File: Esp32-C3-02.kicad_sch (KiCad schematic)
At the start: 0 parts

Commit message: Schematic update
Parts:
- added J3: GSD09002SEU, GSD09002SEU:AMPHENOL_GSD09002SEU, symbol GSD09002SEU:GSD09002SEU
- added U2: USBLC6-2SC6, Package_TO_SOT_SMD:SOT-23-6, symbol Power_Protection:USBLC6-2SC6
- added U3: ESP32-C3-WROOM-02, RF_Module:ESP32-C3-WROOM-02, symbol RF_Module:ESP32-C3-WROOM-02
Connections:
- new net: U3.19 (GND), U3.9 (GND)

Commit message: esp32 circuitry design
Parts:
- removed U3: ESP32-C3-WROOM-02, RF_Module:ESP32-C3-WROOM-02, symbol RF_Module:ESP32-C3-WROOM-02
- added R12: 22.1K, symbol Device:R
- added R13: 47K, symbol Device:R
- added U3: ESP32-C3-WROOM-02-H4, ESP32-C3-WROOM-02-H4:MODULE_ESP32-C3-WROOM-02-H4, symbol ESP32-C3-WROOM-02-H4:ESP32-C3-WROOM-02-H4
- added U4: CP2102N-Axx-xQFN20, Package_DFN_QFN:SiliconLabs_QFN-20-1EP_3x3mm_P0.5mm, symbol Interface_USB:CP2102N-Axx-xQFN20
- added U5: W25Q16JVSS, Package_SO:SOIC-8_5.3x5.3mm_P1.27mm, symbol Memory_Flash:W25Q16JVSS
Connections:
- net at U2.1 (I/O1): now also U4.5 (D-)
- net GND: now reaches U2.2 (GND)
- net at U2.3 (I/O2): now also U4.4 (D+)
- net USB_DP: now reaches U2.4 (I/O2)
- net VBUS: now reaches U2.5 (VBUS)
- net VBUS: now also R12.1
- net USB_DN: now reaches U2.6 (I/O1)
- new net: U4.12 (GND), U4.21 (GND), U4.3 (GND)
- new net: R12.2, R13.1, U4.8 (VBUS)
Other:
- moved on the sheet: J3, U2

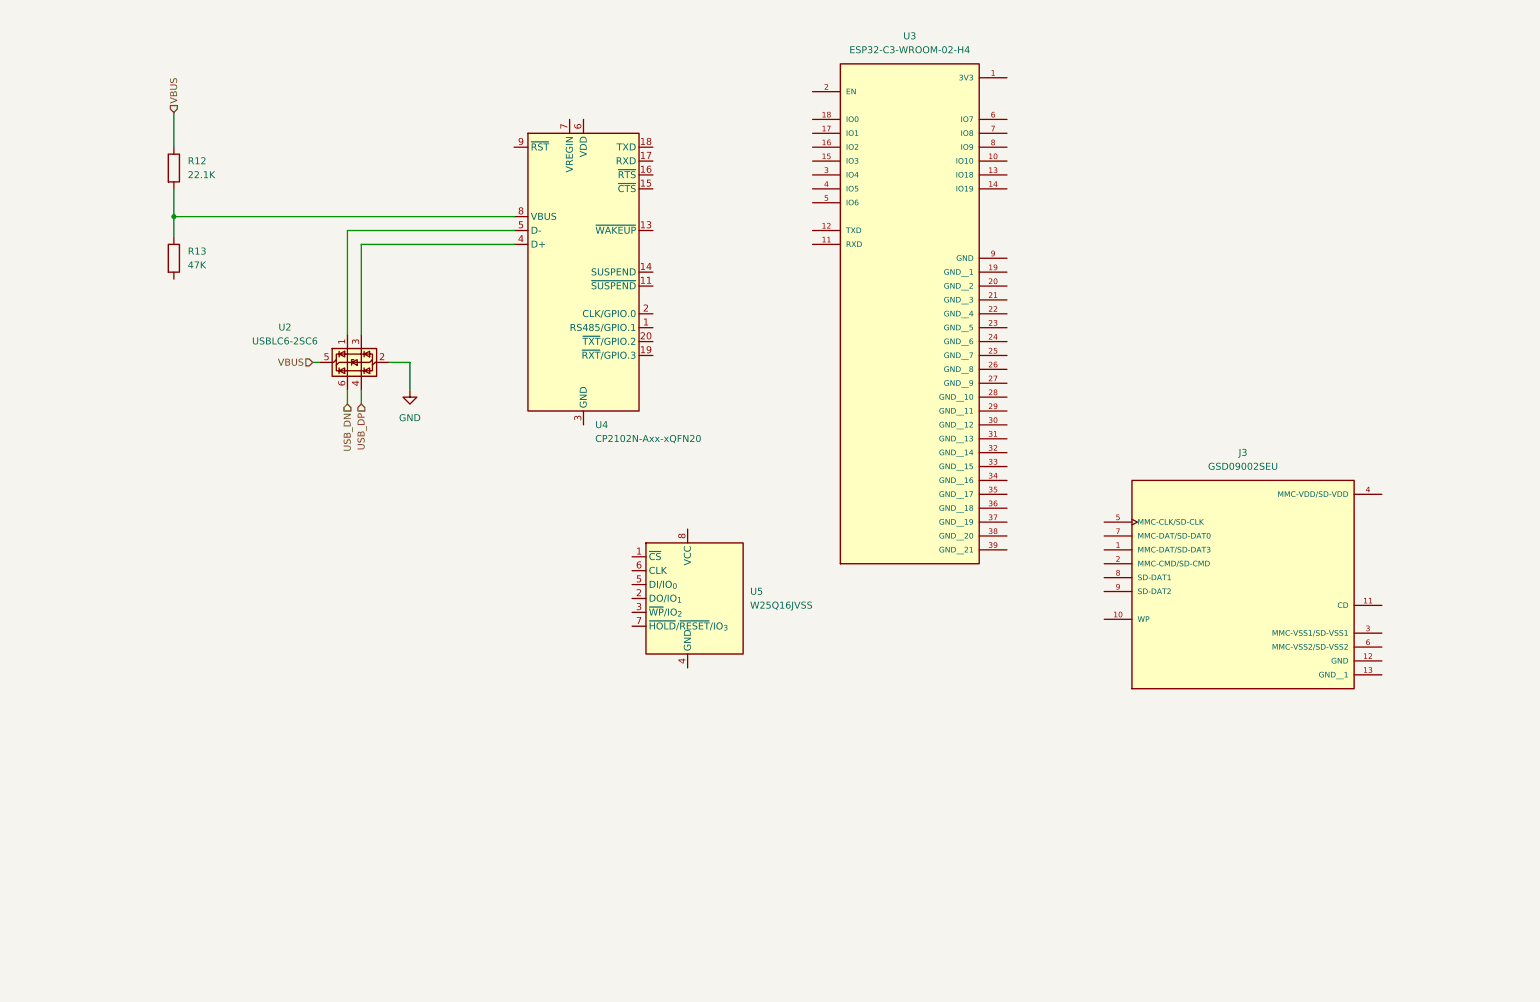
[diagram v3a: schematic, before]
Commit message: update added esp32,uart , sd card and flash memory schematic
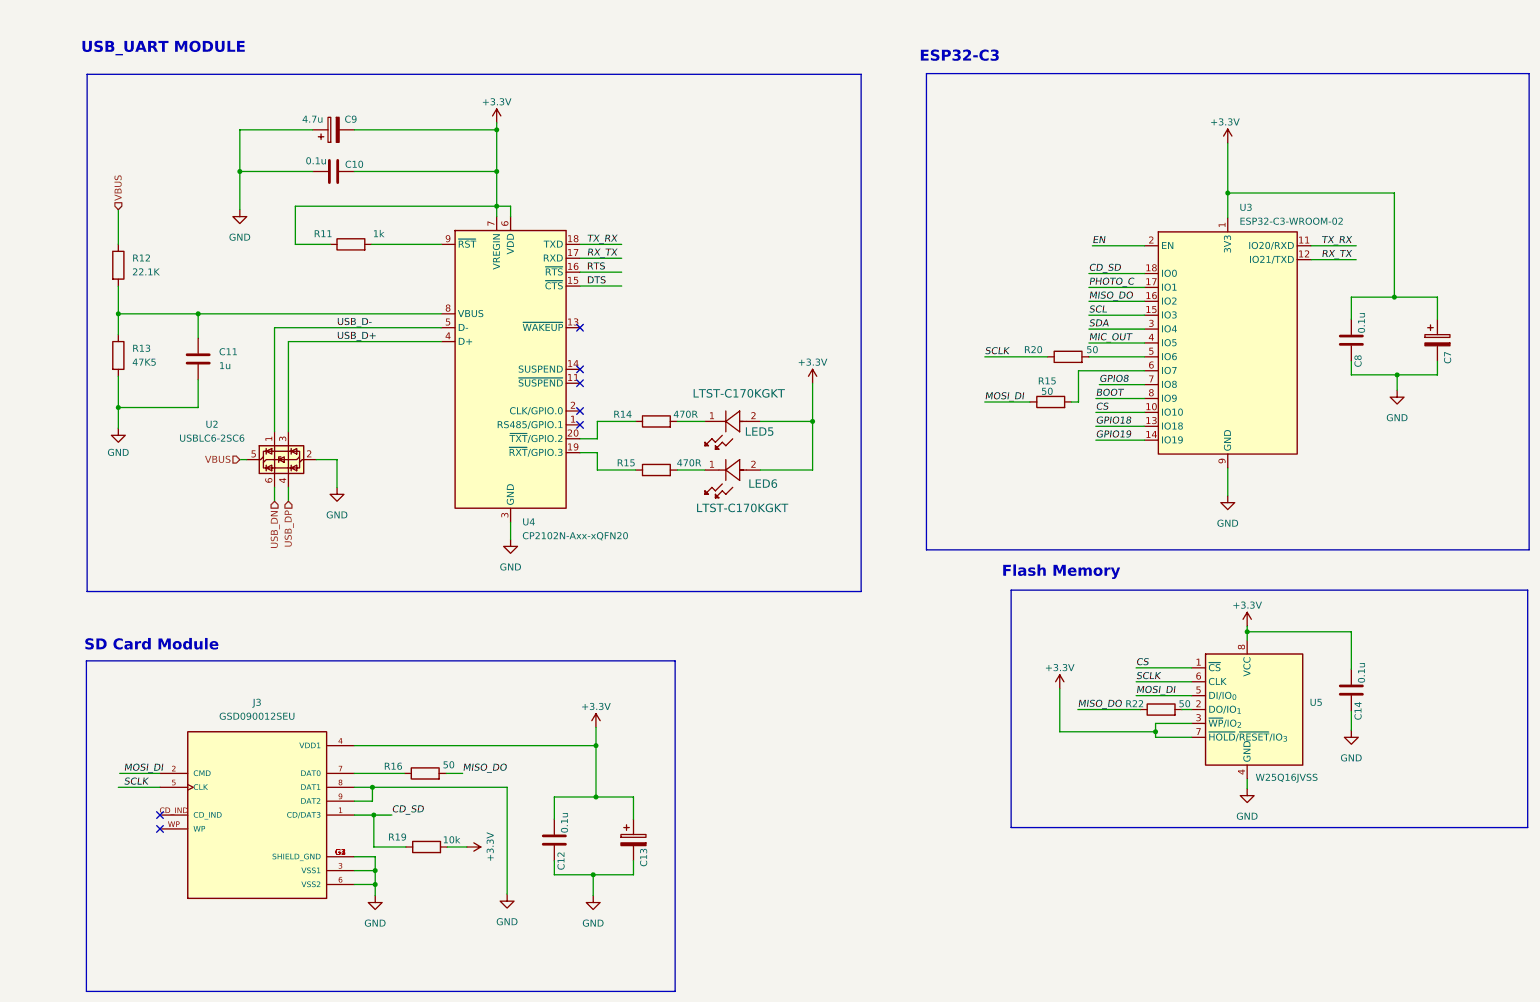
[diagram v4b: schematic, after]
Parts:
- removed J3: GSD09002SEU, GSD09002SEU:AMPHENOL_GSD09002SEU, symbol GSD09002SEU:GSD09002SEU
- removed U3: ESP32-C3-WROOM-02-H4, ESP32-C3-WROOM-02-H4:MODULE_ESP32-C3-WROOM-02-H4, symbol ESP32-C3-WROOM-02-H4:ESP32-C3-WROOM-02-H4
- added C10, C12, C14, C8: 0.1u, symbol Device:C
- added C11: 1u, symbol Device:C
- added C13, C7, C9: 4.7u, symbol Device:C_Polarized
- added J3: GSD090012SEU, GSD090012SEU:AMPHENOL_GSD090012SEU, symbol GSD090012SEU:GSD090012SEU
- added LED5, LED6: LTST-C170KGKT, LED_LTST-C170KGKT_LTO, symbol 2025-07-01_05-12-42:LTST-C170KGKT
- added R11: 1k, symbol Device:R
- added R14, R15: 470R, symbol Device:R
- added R15, R16, R20, R22: 50, symbol Device:R
- added R19: 10k, symbol Device:R
- added U3: ESP32-C3-WROOM-02, RF_Module:ESP32-C3-WROOM-02, symbol RF_Module:ESP32-C3-WROOM-02
- R13: value 47K -> 47K5
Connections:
- net GND: now also R13.2, U4.12 (GND), U4.21 (GND), U4.3 (GND), U5.4 (GND), C10.1, C11.2, C12.2, C13.2, C14.2, C7.2, C8.2, C9.1, J3.3 (VSS1), J3.6 (VSS2), J3.8 (DAT1), J3.9 (DAT2), J3.G1 (SHIELD_GND), J3.G2 (SHIELD_GND), J3.G3 (SHIELD_GND), J3.G4 (SHIELD_GND), U3.19 (GND), U3.9 (GND)
- net USB_D-: now reaches U2.1 (I/O1), U4.5 (D-)
- net USB_D+: now reaches U2.3 (I/O2), U4.4 (D+)
- net DTS: now reaches U4.15 (~{CTS})
- net RTS: now reaches U4.16 (~{RTS})
- net RX_TX: now reaches U4.17 (RXD)
- net RX_TX: now also U3.12 (IO21/TXD)
- net TX_RX: now reaches U4.18 (TXD)
- net TX_RX: now also U3.11 (IO20/RXD)
- net at U4.19 (~{RXT}/GPIO.3): now also R15.1
- net at U4.20 (~{TXT}/GPIO.2): now also R14.1
- net +3.3V: now reaches U4.6 (VDD)
- net +3.3V: now also U4.7 (VREGIN), U5.3 (~{WP}/IO_{2}), U5.7 (~{HOLD}/~{RESET}/IO_{3}), U5.8 (VCC), C10.2, C12.1, C13.1, C14.1, C7.1, C8.1, C9.2, J3.4 (VDD1), LED5.2, LED6.2, R11.1, R19.2, U3.1 (3V3)
- net at R12.2, R13.1, U4.8 (VBUS): now also C11.1
- net at U4.9 (~{RST}): now also R11.2
- net CS: now reaches U5.1 (~{CS})
- net CS: now also U3.10 (IO10)
- net at U5.2 (DO/IO_{1}): now also R22.2
- net MOSI_DI: now reaches U5.5 (DI/IO_{0})
- net MOSI_DI: now also J3.2 (CMD), R15.1
- net SCLK: now reaches U5.6 (CLK)
- net SCLK: now also J3.5 (CLK), R20.1
- new net: LED5.1, R14.2
- new net: J3.7 (DAT0), R16.1
- new net: R20.2, U3.5 (IO6)
- new net: LED6.1, R15.2
- new net: R15.2, U3.6 (IO7)
- new net BOOT: U3.8 (IO9)
- new net CD_SD: J3.1 (CD/DAT3), R19.1, U3.18 (IO0)
- new net EN: U3.2 (EN)
- new net GPIO18: U3.13 (IO18)
- new net GPIO19: U3.14 (IO19)
- new net GPIO8: U3.7 (IO8)
- new net MIC_OUT: U3.4 (IO5)
- new net MISO_DO: R16.2, R22.1, U3.16 (IO2)
- new net PHOTO_C: U3.17 (IO1)
- new net SCL: U3.15 (IO3)
- new net SDA: U3.3 (IO4)
- no-connect marks 0 -> 7
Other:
- note added: "ESP32-C3"
- note added: "Flash Memory"
- note added: "SD Card Module"
- note added: "USB_UART MODULE"
- moved on the sheet: R12, R13, U2, U4, U5

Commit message: final touch on esp32-wroom-02 , flash memory, sd_card,testpoints & USB_UART schematic
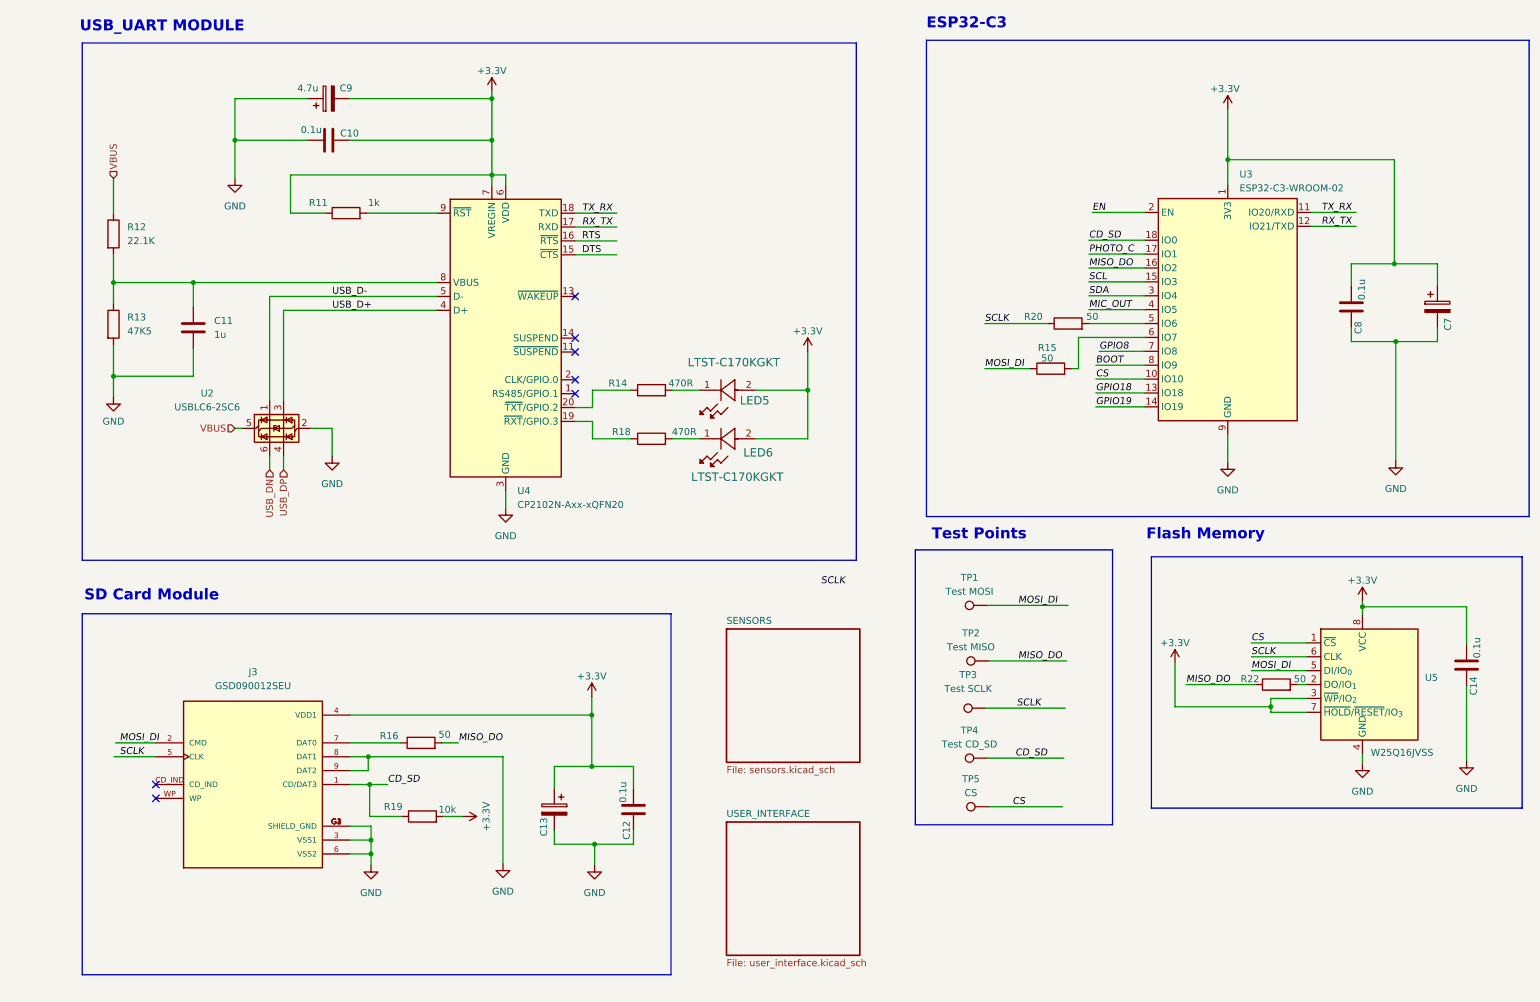
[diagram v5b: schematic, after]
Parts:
- added TP1: Test MOSI, symbol Connector:TestPoint
- added TP2: Test MISO, symbol Connector:TestPoint
- added TP3: Test SCLK, symbol Connector:TestPoint
- added TP4: Test CD_SD, symbol Connector:TestPoint
- added TP5: CS, symbol Connector:TestPoint
- renumbered R15 to R18
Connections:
- net CD_SD: now also TP4.1
- net CS: now also TP5.1
- net MISO_DO: now also TP2.1
- net MOSI_DI: now also TP1.1
- net SCLK: now also TP3.1
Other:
- added sheet SENSORS (sensors.kicad_sch)
- added sheet USER_INTERFACE (user_interface.kicad_sch)
- note added: "Test Points"
- company: (none) -> #OdariDesigns
- title: (none) -> ESP32,SD_CARD,FLASH_MEMORY &USB_UART_MODULE
- moved on the sheet: C10, C11, C12, C13, C14, C7, C8, C9, J3, LED5, LED6, R11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

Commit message: connecting hierarchial Pins
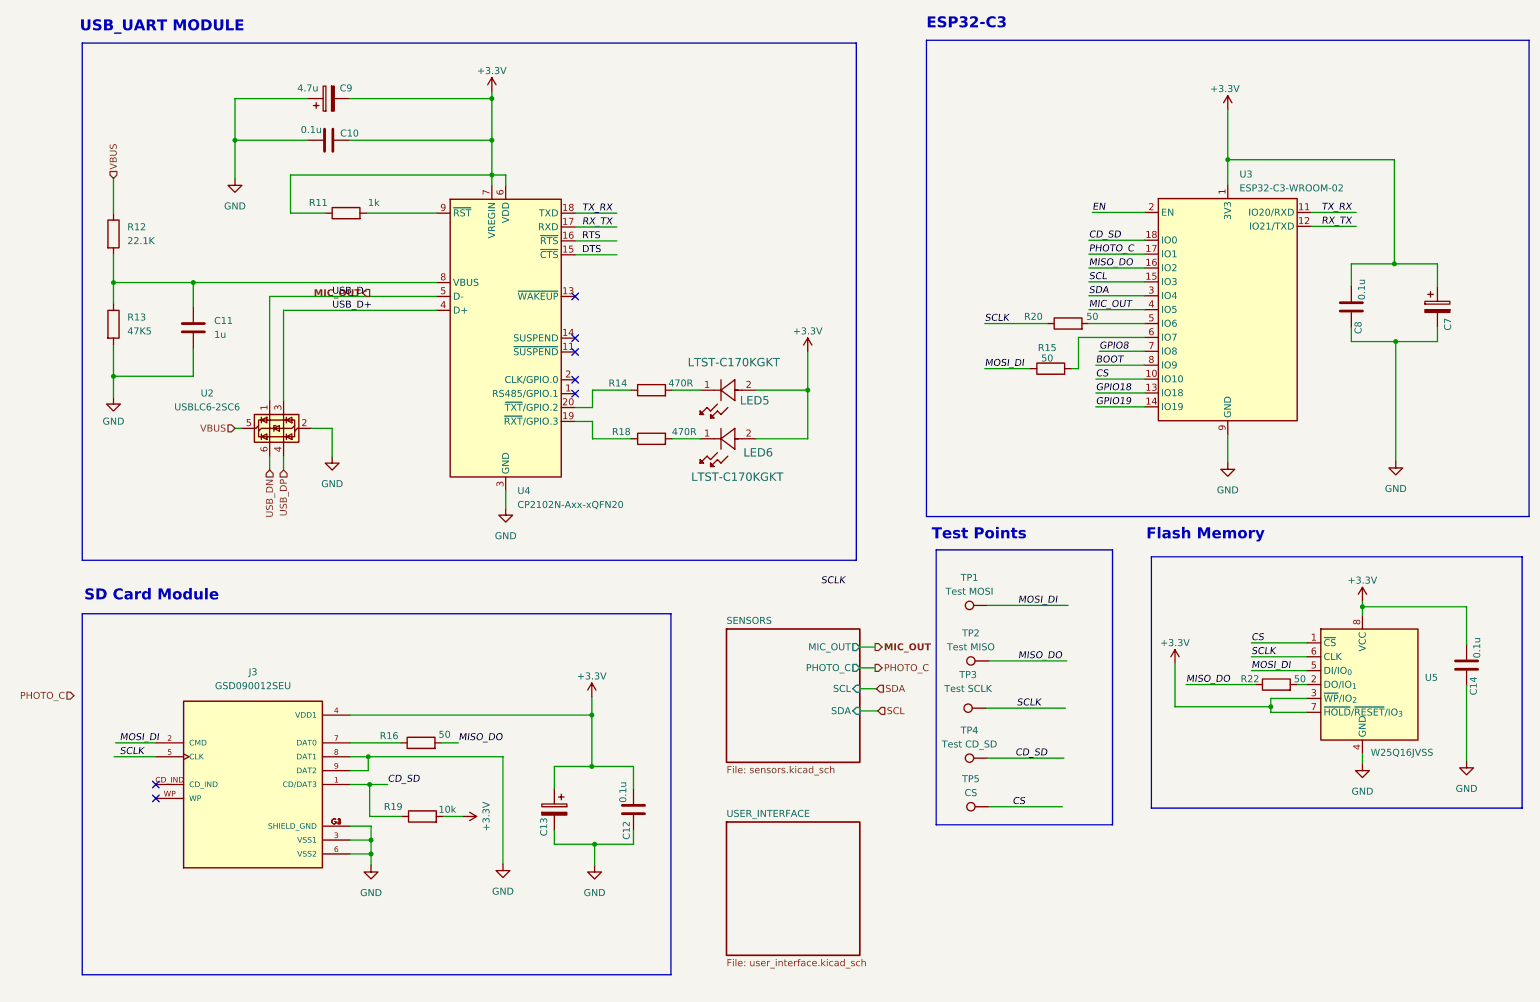
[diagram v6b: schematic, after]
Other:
- sheet SENSORS ports: added MIC_OUT, PHOTO_C, SCL, SDA; removed none
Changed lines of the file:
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@@
 	)
 	(rectangle
-		(start 167.386 113.03)
+		(start 171.196 113.03)
 		(end 203.454 163.322)
 		(stroke
@@
 	(wire
 		(pts
+			(xy 157.226 142.494) (xy 160.528 142.494)
+		)
+		(stroke
+			(width 0)
+			(type default)
+		)
+	)
+	(wire
+		(pts
 			(xy 53.086 44.45) (xy 89.916 44.45)
 		)
@@
 	(wire
 		(pts
+			(xy 157.226 134.62) (xy 160.02 134.62)
+		)
+		(stroke
+			(width 0)
+			(type default)
+		)
+	)
+	(wire
+		(pts
 			(xy 228.854 135.128) (xy 239.014 135.128)
 		)
@@
 	(wire
 		(pts
+			(xy 157.226 138.43) (xy 160.274 138.43)
+		)
+		(stroke
+			(width 0)
+			(type default)
+		)
+	)
+	(wire
+		(pts
 			(xy 249.174 123.444) (xy 249.174 124.968)
 		)
@@
 	(wire
 		(pts
+			(xy 157.226 130.81) (xy 160.02 130.81)
+		)
+		(stroke
+			(width 0)
+			(type default)
+		)
+	)
+	(wire
+		(pts
 			(xy 180.848 133.35) (xy 195.072 133.35)
 		)
@@
 		)
 	)
+	(hierarchical_label "PHOTO_C"
+		(shape input)
+		(at 13.462 139.7 180)
+		(effects
+			(font
+				(size 1.27 1.27)
+			)
+			(justify right)
+		)
+	)
+	(hierarchical_label "MIC_OUT"
+		(shape output)
+		(at 67.564 66.04 180)
+		(effects
+			(font
+				(size 1.27 1.27)
+				(thickness 0.254)
+				(bold yes)
+			)
+			(justify right)
+		)
+	)
 	(hierarchical_label "USB_DN"
 		(shape input)
@@
 		)
 	)
+	(hierarchical_label "SDA"
+		(shape input)
+		(at 160.274 138.43 0)
+		(effects
+			(font
+				(size 1.27 1.27)
+			)
+			(justify left)
+		)
+	)
 	(hierarchical_label "VBUS"
 		(shape input)
@@
 		)
 	)
+	(hierarchical_label "MIC_OUT"
+		(shape output)
+		(at 160.02 130.81 0)
+		(effects
+			(font
+				(size 1.27 1.27)
+				(thickness 0.254)
+				(bold yes)
+			)
+			(justify left)
+		)
+	)
+	(hierarchical_label "SCL"
+		(shape input)
+		(at 160.528 142.494 0)
+		(effects
+			(font
+				(size 1.27 1.27)
+			)
+			(justify left)
+		)
+	)
+	(hierarchical_label "PHOTO_C"
+		(shape output)
+		(at 160.02 134.62 0)
+		(effects
+			(font
+				(size 1.27 1.27)
+			)
+			(justify left)
+		)
+	)
 	(symbol
 		(lib_id "Device:R")
@@
 			)
 		)
+		(pin "MIC_OUT" output
+			(at 157.226 130.81 0)
+			(effects
+				(font
+					(size 1.27 1.27)
+				)
+				(justify right)
+			)
+		)
+		(pin "SCL" input
+			(at 157.226 138.43 0)
+			(effects
+				(font
+					(size 1.27 1.27)
+				)
+				(justify right)
+			)
+		)
+		(pin "SDA" input
+			(at 157.226 142.494 0)
+			(effects
+				(font
+					(size 1.27 1.27)
+				)
+				(justify right)
+			)
+		)
+		(pin "PHOTO_C" output
+			(at 157.226 134.62 0)
+			(effects
+				(font
+					(size 1.27 1.27)
+				)
+				(justify right)
+			)
+		)

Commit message: update the mcu sheet
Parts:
- C12: renamed from C13; value 4.7u -> 10u
- C13: renamed from C12; value 0.1u -> 4.7u
- C7: value 4.7u -> 10u
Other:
- sheet SENSORS renamed Sensor_sheet
- sheet USER_INTERFACE renamed user_interface_sheet
- sheet user_interface_sheet ports: added BOOT, DTR, EN, GPIO18, GPIO19, GPIO8, RTS, SCL, SDA; removed none
- moved on the sheet: R15, R20
